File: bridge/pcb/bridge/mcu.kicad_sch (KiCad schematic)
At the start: 26 parts, among them J11 5V_Enable, J5 Conn_01x04, J6 Conn_01x02, J7 Conn_01x03, J8 Conn_01x02, J9 MCU_Test_Point, U1 L293, U3 AD557JN, U4 ATmega328P-P, U5 L7805

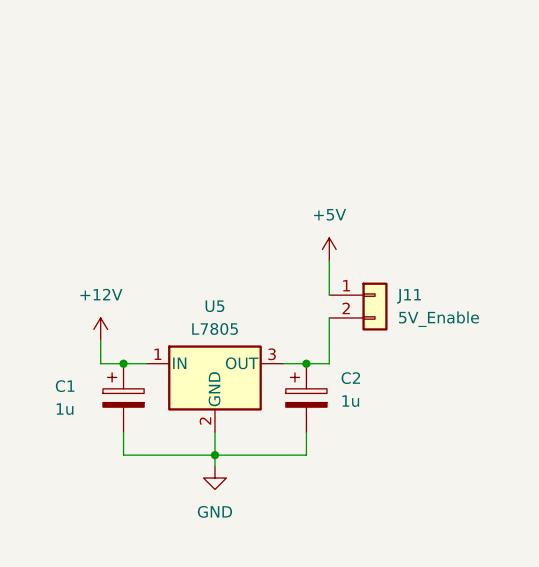
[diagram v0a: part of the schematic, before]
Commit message: Assigned footprints and layed out board
Removed 5V and 12V enable headers as they added unneeded complexity
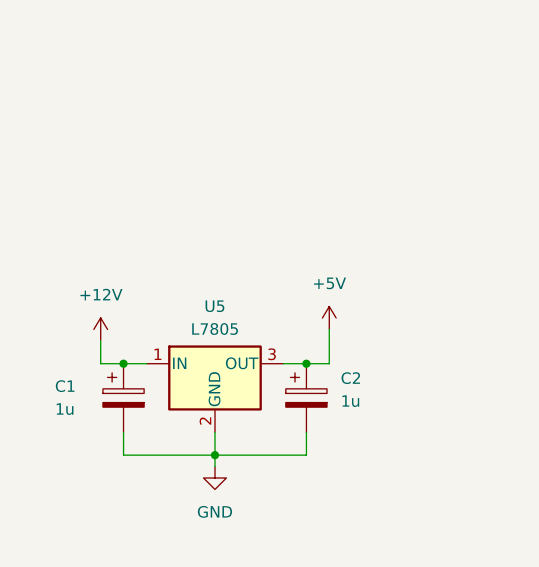
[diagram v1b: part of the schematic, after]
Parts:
- removed J11: 5V_Enable, Connector_PinHeader_2.54mm:PinHeader_1x02_P2.54mm_Vertical, symbol Connector_Generic:Conn_01x02
- C1, C2, C3, C4: footprint (none) -> Capacitor_THT:CP_Radial_D5.0mm_P2.00mm
- U5: footprint (none) -> Package_TO_SOT_THT:TO-220-3_Horizontal_TabDown
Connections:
- net +5V: now also C2.1, U5.3 (OUT)
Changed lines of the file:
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@@
     (stroke (width 0) (type default))
   )
-  (wire (pts (xy 257.81 49.53) (xy 257.81 53.34))
+  (wire (pts (xy 257.81 57.15) (xy 257.81 60.96))
     (stroke (width 0) (type default))
   )
   (wire (pts (xy 48.26 25.4) (xy 48.26 24.13))
-    (stroke (width 0) (type default))
-  )
-  (wire (pts (xy 257.81 55.88) (xy 257.81 60.96))
     (stroke (width 0) (type default))
   )
@@
     )
   )
-  (symbol (lib_id "Connector_Generic:Conn_01x02") (at 262.89 53.34 0) (unit 1)
-    (in_bom yes) (on_board yes) (dnp no) (fields_autoplaced)
-    (property "Reference" "J11" (at 265.43 53.34 0)
-      (effects (font (size 1.27 1.27)) (justify left))
-    )
-    (property "Value" "5V_Enable" (at 265.43 55.88 0)
-      (effects (font (size 1.27 1.27)) (justify left))
-    )
-    (property "Footprint" "Connector_PinHeader_2.54mm:PinHeader_1x02_P2.54mm_Vertical" (at 262.89 53.34 0)
-      (effects (font (size 1.27 1.27)) hide)
-    )
-    (property "Datasheet" "~" (at 262.89 53.34 0)
-      (effects (font (size 1.27 1.27)) hide)
-    )
-    (pin "1")
-    (pin "2")
-    (instances
-      (project "bridge"
-        (path "/40a0f45e-7290-47b9-8da3-09f7dfbfbbd7/00f451ee-7b68-4840-8f31-2bfc247688fa"
-          (reference "J11") (unit 1)
-        )
-      )
-    )
-  )
   (symbol (lib_id "power:GND") (at 45.72 102.87 0) (unit 1)
     (in_bom yes) (on_board yes) (dnp no) (fields_autoplaced)
@@
       (effects (font (size 1.27 1.27)) (justify left))
     )
-    (property "Footprint" "" (at 70.8152 26.67 0)
+    (property "Footprint" "Capacitor_THT:CP_Radial_D5.0mm_P2.00mm" (at 70.8152 26.67 0)
       (effects (font (size 1.27 1.27)) hide)
     )
@@
       (effects (font (size 1.27 1.27)) (justify left))
     )
-    (property "Footprint" "" (at 195.2752 62.23 0)
+    (property "Footprint" "Capacitor_THT:CP_Radial_D5.0mm_P2.00mm" (at 195.2752 62.23 0)
       (effects (font (size 1.27 1.27)) hide)
     )
@@
       (effects (font (size 1.27 1.27)))
     )
-    (property "Footprint" "" (at 245.745 64.77 0)
+    (property "Footprint" "Package_TO_SOT_THT:TO-220-3_Horizontal_TabDown" (at 245.745 64.77 0)
       (effects (font (size 1.27 1.27) italic) (justify left) hide)
     )
@@
     )
   )
-  (symbol (lib_id "power:+5V") (at 257.81 49.53 0) (unit 1)
-    (in_bom yes) (on_board yes) (dnp no) (fields_autoplaced)
-    (property "Reference" "#PWR010" (at 257.81 53.34 0)
-      (effects (font (size 1.27 1.27)) hide)
-    )
-    (property "Value" "+5V" (at 257.81 44.45 0)
-      (effects (font (size 1.27 1.27)))
-    )
-    (property "Footprint" "" (at 257.81 49.53 0)
-      (effects (font (size 1.27 1.27)) hide)
-    )
-    (property "Datasheet" "" (at 257.81 49.53 0)
+  (symbol (lib_id "power:+5V") (at 257.81 57.15 0) (unit 1)
+    (in_bom yes) (on_board yes) (dnp no) (fields_autoplaced)
+    (property "Reference" "#PWR010" (at 257.81 60.96 0)
+      (effects (font (size 1.27 1.27)) hide)
+    )
+    (property "Value" "+5V" (at 257.81 52.07 0)
+      (effects (font (size 1.27 1.27)))
+    )
+    (property "Footprint" "" (at 257.81 57.15 0)
+      (effects (font (size 1.27 1.27)) hide)
+    )
+    (property "Datasheet" "" (at 257.81 57.15 0)
       (effects (font (size 1.27 1.27)) hide)
     )
@@
       (effects (font (size 1.27 1.27)) (justify left))
     )
-    (property "Footprint" "" (at 235.9152 68.58 0)
+    (property "Footprint" "Capacitor_THT:CP_Radial_D5.0mm_P2.00mm" (at 235.9152 68.58 0)
       (effects (font (size 1.27 1.27)) hide)
     )
@@
       (effects (font (size 1.27 1.27)) (justify left))
     )
-    (property "Footprint" "" (at 256.2352 68.58 0)
-      (effects (font (size 1.27 1.27)) hide)
-    )
+    (property "Footprint" "Capacitor_THT:CP_Radial_D5.0mm_P2.00mm" (at 256.2352 68.58 0)
+      (effects (font (size 1.27 1.27)) hide)
+    )

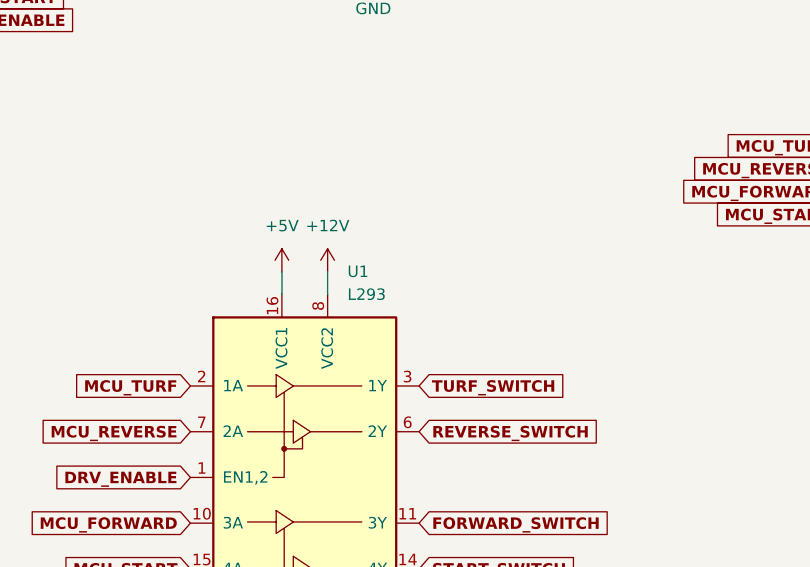
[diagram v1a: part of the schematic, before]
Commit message: Added extra capacitor for L293
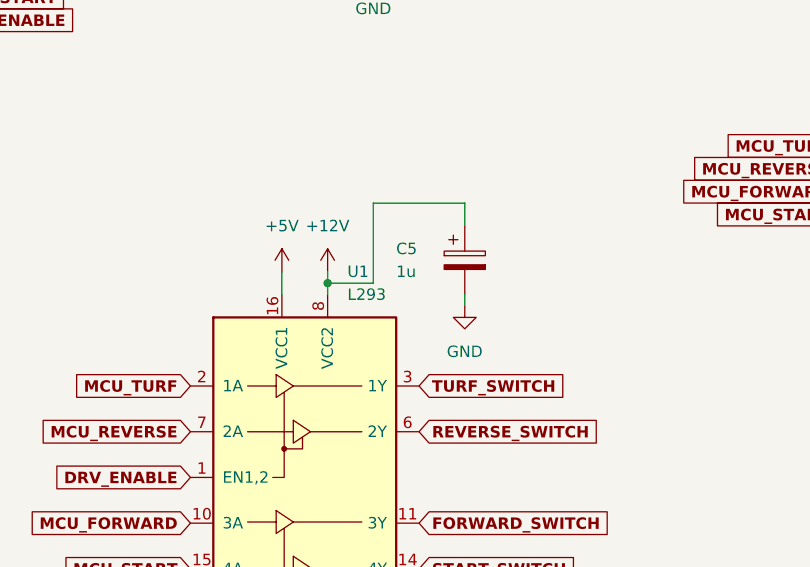
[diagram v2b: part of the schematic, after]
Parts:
- added C5: 1u, Capacitor_THT:CP_Radial_D5.0mm_P2.00mm, symbol Device:C_Polarized
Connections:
- net +12V: now also C5.1
- net GND: now also C5.2
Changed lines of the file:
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@@
   (junction (at 189.23 57.15) (diameter 0) (color 0 0 0 0)
+  )
+  (junction (at 104.14 120.65) (diameter 0) (color 0 0 0 0)
   )
   (junction (at 194.31 54.61) (diameter 0) (color 0 0 0 0)
@@
     (stroke (width 0) (type default))
   )
+  (wire (pts (xy 104.14 120.65) (xy 109.22 120.65))
+    (stroke (width 0) (type default))
+  )
   (wire (pts (xy 60.96 40.64) (xy 78.74 40.64))
     (stroke (width 0) (type default))
@@
     (stroke (width 0) (type default))
   )
-  (wire (pts (xy 104.14 119.38) (xy 104.14 121.92))
+  (wire (pts (xy 104.14 119.38) (xy 104.14 120.65))
     (stroke (width 0) (type default))
   )
@@
     (stroke (width 0) (type default))
   )
+  (wire (pts (xy 119.38 121.92) (xy 119.38 123.19))
+    (stroke (width 0) (type default))
+  )
   (wire (pts (xy 104.14 167.64) (xy 104.14 171.45))
     (stroke (width 0) (type default))
@@
     (stroke (width 0) (type default))
   )
+  (wire (pts (xy 104.14 120.65) (xy 104.14 121.92))
+    (stroke (width 0) (type default))
+  )
   (wire (pts (xy 60.96 38.1) (xy 76.2 38.1))
     (stroke (width 0) (type default))
@@
     (stroke (width 0) (type default))
   )
+  (wire (pts (xy 119.38 114.3) (xy 119.38 111.76))
+    (stroke (width 0) (type default))
+  )
   (wire (pts (xy 82.55 66.04) (xy 82.55 64.77))
     (stroke (width 0) (type default))
@@
     (stroke (width 0) (type default))
   )
+  (wire (pts (xy 119.38 111.76) (xy 109.22 111.76))
+    (stroke (width 0) (type default))
+  )
   (wire (pts (xy 233.68 147.32) (xy 233.68 151.13))
     (stroke (width 0) (type default))
@@
   )
   (wire (pts (xy 48.26 25.4) (xy 48.26 24.13))
+    (stroke (width 0) (type default))
+  )
+  (wire (pts (xy 109.22 111.76) (xy 109.22 120.65))
     (stroke (width 0) (type default))
   )
@@
     (property "Intersheetrefs" "${INTERSHEET_REFS}" (at 79.6612 63.5 0)
       (effects (font (size 1.27 1.27)) (justify left) hide)
+    )
+  )
+  (symbol (lib_id "Device:C_Polarized") (at 119.38 118.11 0) (unit 1)
+    (in_bom yes) (on_board yes) (dnp no)
+    (property "Reference" "C5" (at 111.76 116.84 0)
+      (effects (font (size 1.27 1.27)) (justify left))
+    )
+    (property "Value" "1u" (at 111.76 119.38 0)
+      (effects (font (size 1.27 1.27)) (justify left))
+    )
+    (property "Footprint" "Capacitor_THT:CP_Radial_D5.0mm_P2.00mm" (at 120.3452 121.92 0)
+      (effects (font (size 1.27 1.27)) hide)
+    )
+    (property "Datasheet" "~" (at 119.38 118.11 0)
+      (effects (font (size 1.27 1.27)) hide)
+    )
+    (pin "2")
+    (pin "1")
+    (instances
+      (project "bridge"
+        (path "/40a0f45e-7290-47b9-8da3-09f7dfbfbbd7/00f451ee-7b68-4840-8f31-2bfc247688fa"
+          (reference "C5") (unit 1)
+        )
+      )
     )
   )
@@
         )
       )
+    )
+  )
+  (symbol (lib_id "power:GND") (at 119.38 123.19 0) (unit 1)
+    (in_bom yes) (on_board yes) (dnp no) (fields_autoplaced)
+    (property "Reference" "#PWR041" (at 119.38 129.54 0)
+      (effects (font (size 1.27 1.27)) hide)
+    )
+    (property "Value" "GND" (at 119.38 128.27 0)
+      (effects (font (size 1.27 1.27)))
+    )
+    (property "Footprint" "" (at 119.38 123.19 0)
+      (effects (font (size 1.27 1.27)) hide)
+    )
+    (property "Datasheet" "" (at 119.38 123.19 0)
+      (effects (font (size 1.27 1.27)) hide)
+    )
+    (pin "1")
+    (instances
+      (project "bridge"
+        (path "/40a0f45e-7290-47b9-8da3-09f7dfbfbbd7/00f451ee-7b68-4840-8f31-2bfc247688fa"
+          (reference "#PWR041") (unit 1)
+        )
+      )

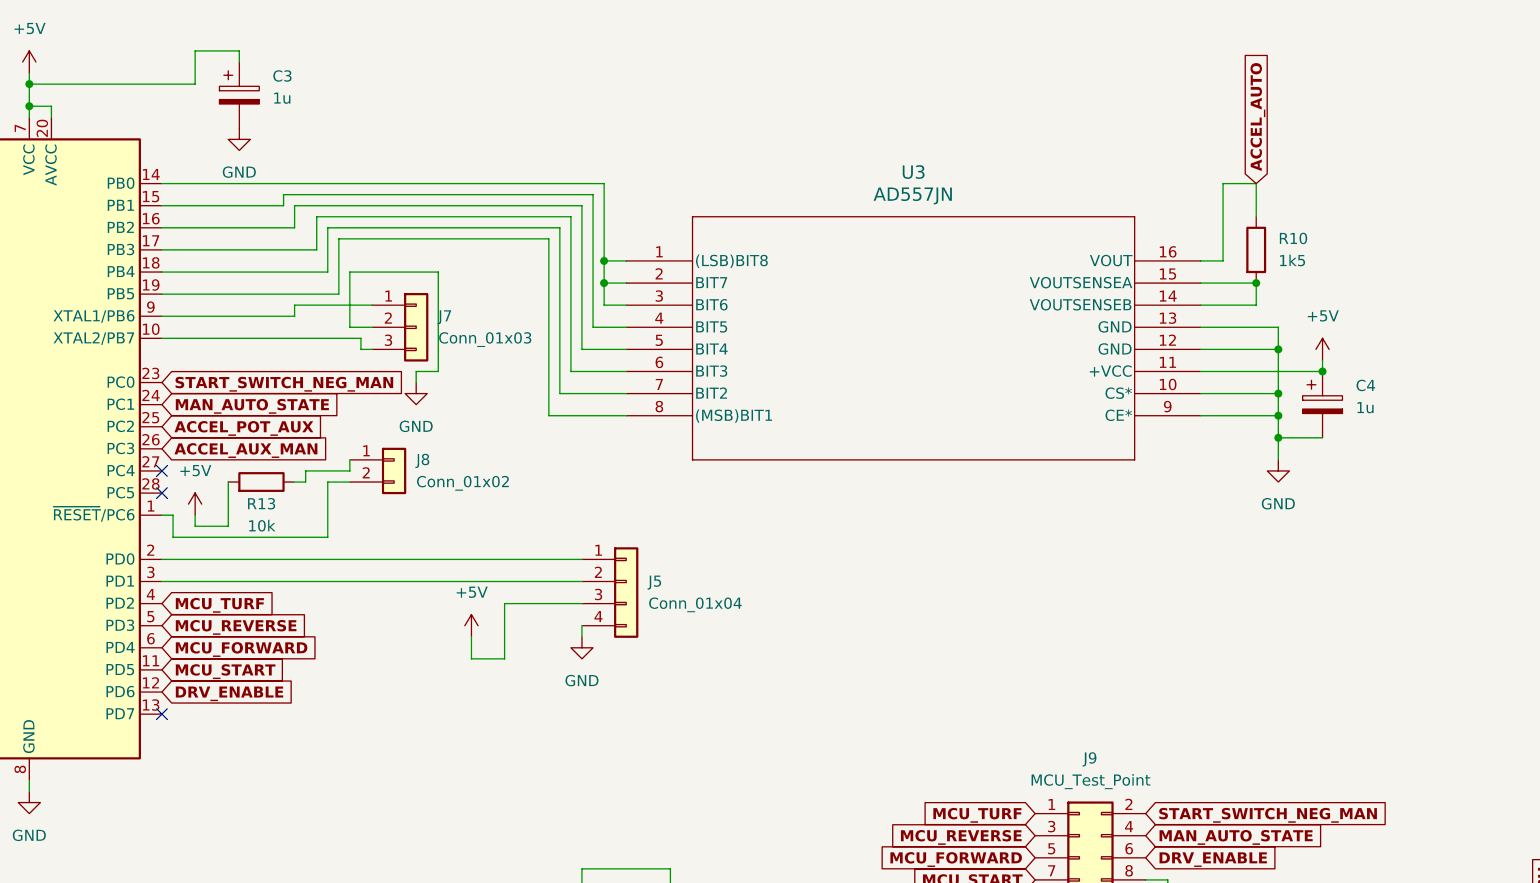
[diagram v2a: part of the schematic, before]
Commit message: Changed DAC to MCP4901
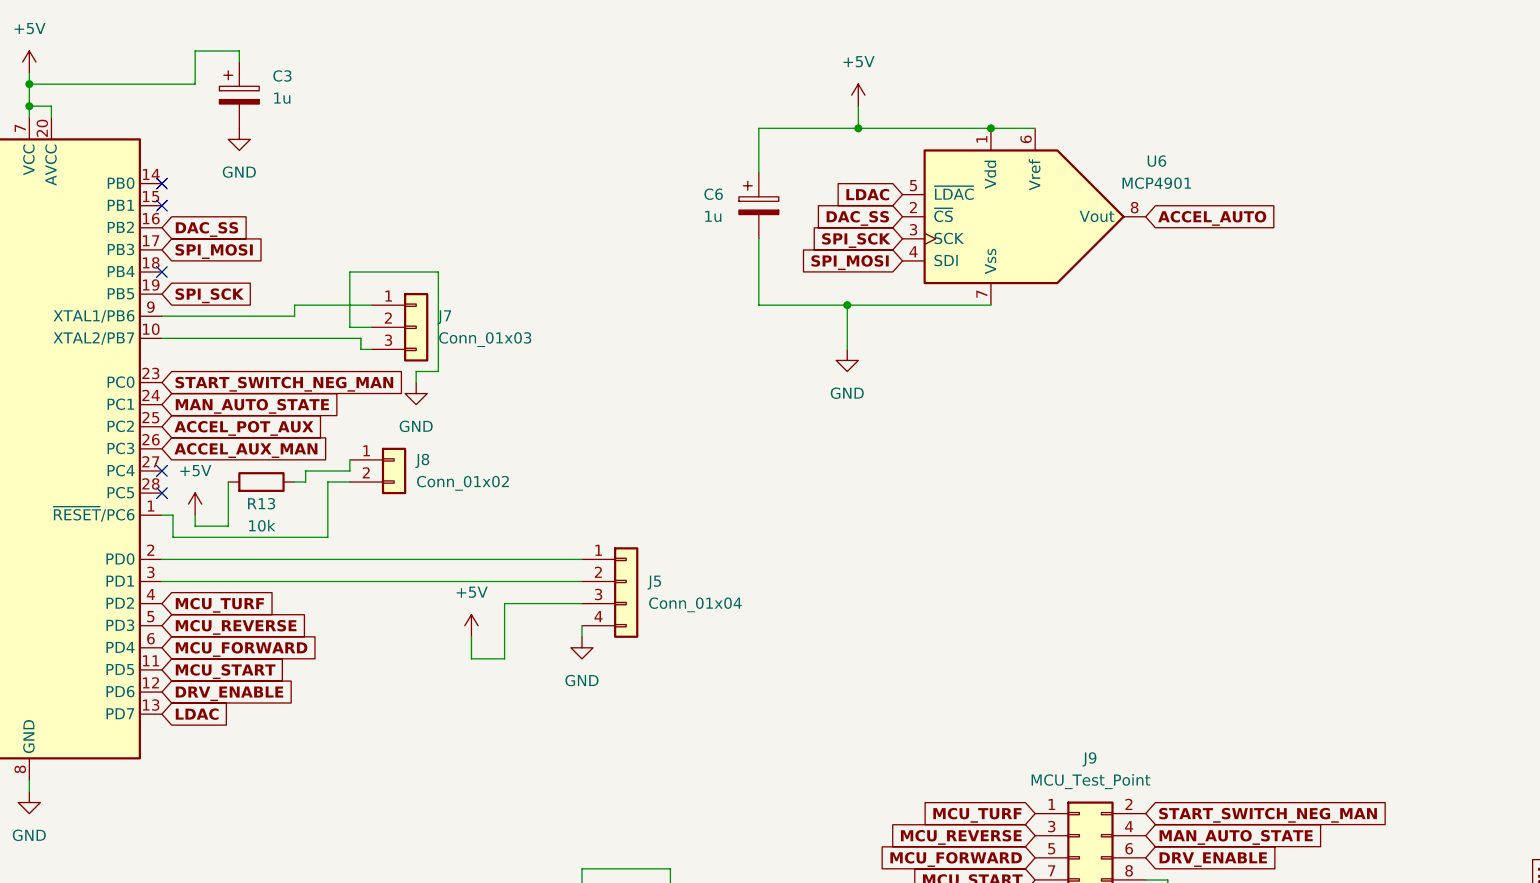
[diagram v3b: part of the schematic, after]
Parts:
- removed C4: 1u, Capacitor_THT:CP_Radial_D5.0mm_P2.00mm, symbol Device:C_Polarized
- removed R10: 1k5, bridge:THT_RESISTOR_WITH_VALUE, symbol Device:R
- removed U3: AD557JN, bridge:AD557JN, symbol bridge:AD557JN
- added C6: 1u, Capacitor_THT:CP_Radial_D5.0mm_P2.00mm, symbol Device:C_Polarized
- added U6: MCP4901, symbol Analog_DAC:MCP4901
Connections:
- net +5V: now also C6.1, U6.1 (Vdd), U6.6 (Vref)
- net ACCEL_AUTO: now also U6.8 (Vout)
- net GND: now also C6.2, U6.7 (Vss)
- net LDAC: now reaches U4.13 (PD7)
- net LDAC: now also U6.5 (~{LDAC})
- net DAC_SS: now reaches U4.16 (PB2)
- net DAC_SS: now also U6.2 (~{CS})
- net SPI_MOSI: now reaches U4.17 (PB3)
- net SPI_MOSI: now also U6.4 (SDI)
- net SPI_SCK: now reaches U4.19 (PB5)
- net SPI_SCK: now also U6.3 (SCK)
- no-connect marks 4 -> 6
